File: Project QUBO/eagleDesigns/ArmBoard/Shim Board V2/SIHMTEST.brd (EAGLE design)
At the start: 71.1 x 81.3 mm, 30 parts, among them IC1 MCP2551/SN, U1 BME280

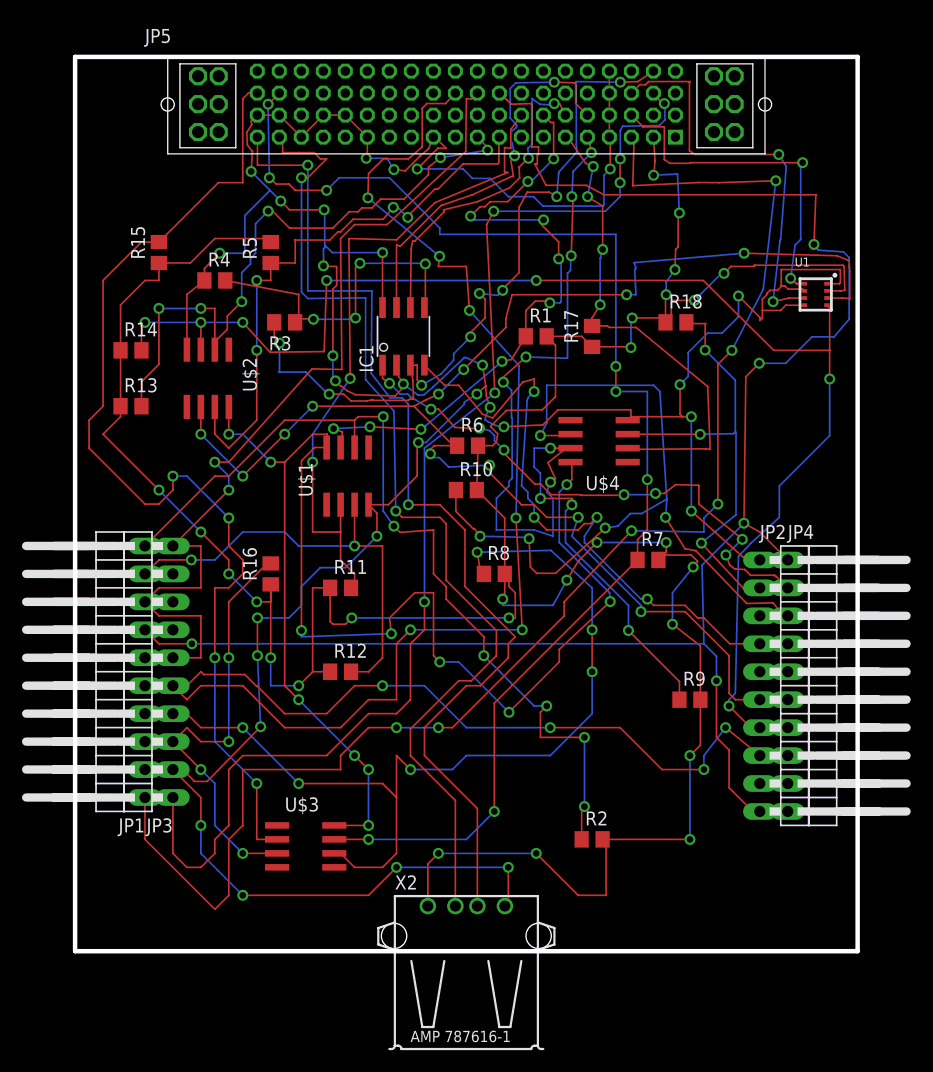
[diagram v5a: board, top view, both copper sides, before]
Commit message: 
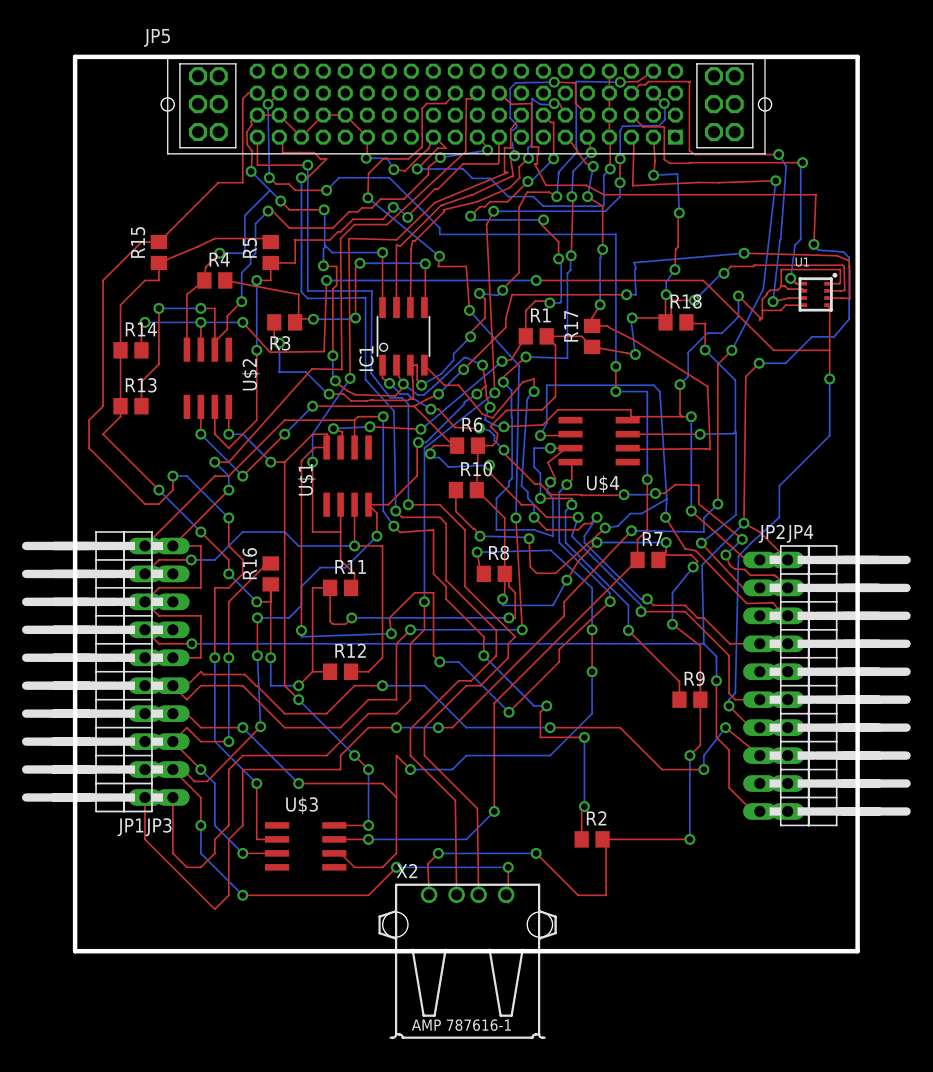
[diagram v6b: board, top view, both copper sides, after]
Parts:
- moved X2 1.04 mm to (35.7, -7.86)
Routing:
- net USB-: track 92.9 -> 91.9 mm
- net USB+: track 94.1 -> 93.0 mm
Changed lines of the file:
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@@
 <attribute name="PROD_ID" value="IC-13090" x="67.31" y="59.69" size="1.778" layer="27" display="off"/>
 </element>
-<element name="X2" library="con-amp" package="USB" value="" x="35.56" y="-8.89"/>
+<element name="X2" library="con-amp" package="USB" value="" x="35.6743" y="-7.8613"/>
 </elements>
 <signals>
@@
 <contactref element="X2" pad="3"/>
 <contactref element="JP5" pad="20"/>
-<wire x1="36.56" y1="4.1001" x2="36.56" y2="12.97" width="0.1524" layer="1"/>
+<wire x1="36.6743" y1="5.1288" x2="36.56" y2="12.97" width="0.1524" layer="1"/>
 <wire x1="36.56" y1="12.97" x2="31.75" y2="17.78" width="0.1524" layer="1"/>
 <wire x1="31.75" y1="17.78" x2="31.75" y2="20.32" width="0.1524" layer="1"/>
@@
 <contactref element="X2" pad="2"/>
 <contactref element="JP5" pad="19"/>
-<wire x1="34.56" y1="4.1001" x2="34.56" y2="13.7" width="0.1524" layer="1"/>
+<wire x1="34.6743" y1="5.1288" x2="34.56" y2="13.7" width="0.1524" layer="1"/>
 <wire x1="34.56" y1="13.7" x2="30.48" y2="17.78" width="0.1524" layer="1"/>
 <wire x1="30.48" y1="17.78" x2="30.48" y2="20.193" width="0.1524" layer="1"/>
@@
 <wire x1="6.35" y1="60.96" x2="7.62" y2="60.96" width="0.1524" layer="1"/>
 <wire x1="7.62" y1="60.96" x2="7.62" y2="62.55" width="0.1524" layer="1"/>
-<wire x1="7.62" y1="62.55" x2="10.48" y2="62.55" width="0.1524" layer="1"/>
-<wire x1="10.48" y1="62.55" x2="12.7" y2="64.77" width="0.1524" layer="1"/>
+<wire x1="7.62" y1="62.55" x2="11.1658" y2="64.0359" width="0.1524" layer="1"/>
+<wire x1="11.1658" y1="64.0359" x2="12.7" y2="64.77" width="0.1524" layer="1"/>
 <wire x1="12.7" y1="64.77" x2="17.36" y2="64.77" width="0.1524" layer="1"/>
 <wire x1="4.13" y1="49.53" x2="4.13" y2="48.58" width="0.1524" layer="1"/>
@@
 <wire x1="17.78" y1="31.75" x2="17.78" y2="33.34" width="0.1524" layer="1"/>
 <wire x1="4.13" y1="49.53" x2="4.13" y2="54.61" width="0.1524" layer="1"/>
-<wire x1="32.0599" y1="4.1001" x2="32.0599" y2="7.9299" width="0.1524" layer="1"/>
+<wire x1="32.1742" y1="5.1288" x2="32.0599" y2="7.9299" width="0.1524" layer="1"/>
 <wire x1="32.0599" y1="7.9299" x2="33.02" y2="8.89" width="0.1524" layer="1"/>
 <via x="33.02" y="8.89" extent="1-16" drill="0.6"/>
@@
 <wire x1="69.78015" y1="62.35065" x2="61.77915" y2="62.35065" width="0.1524" layer="1"/>
 <wire x1="61.77915" y1="62.35065" x2="61.66485" y2="62.23635" width="0.1524" layer="1"/>
-<wire x1="46.99" y1="54.93" x2="50.4546" y2="54.93" width="0.1524" layer="1"/>
-<wire x1="50.4546" y1="54.93" x2="50.5206" y2="54.864" width="0.1524" layer="1"/>
-<via x="50.5206" y="54.864" extent="1-16" drill="0.6"/>
-<wire x1="50.5206" y1="54.864" x2="50.5206" y2="57.43575" width="0.1524" layer="16"/>
+<wire x1="46.99" y1="54.93" x2="50.16885" y2="54.3585" width="0.1524" layer="1"/>
+<wire x1="50.16885" y1="54.3585" x2="50.92065" y2="54.23535" width="0.1524" layer="1"/>
+<via x="50.92065" y="54.23535" extent="1-16" drill="0.6"/>
+<wire x1="50.92065" y1="54.23535" x2="50.5206" y2="57.43575" width="0.1524" layer="16"/>
 <wire x1="50.5206" y1="57.43575" x2="50.6349" y2="57.55005" width="0.1524" layer="16"/>
 <via x="50.6349" y="57.55005" extent="1-16" drill="0.6"/>
@@
 <via x="39.37" y="7.62" extent="1-16" drill="0.6"/>
 <wire x1="39.37" y1="7.62" x2="39.37" y2="4.41" width="0.1524" layer="1"/>
-<wire x1="39.37" y1="4.41" x2="39.0601" y2="4.1001" width="0.1524" layer="1"/>
+<wire x1="39.37" y1="4.41" x2="39.1744" y2="5.1288" width="0.1524" layer="1"/>
 <wire x1="10.16" y1="54.67" x2="10.16" y2="59.69" width="0.1524" layer="1"/>
 <wire x1="10.16" y1="59.69" x2="11.75" y2="60.96" width="0.1524" layer="1"/>
@@
 <wire x1="27.432" y1="37.719" x2="27.432" y2="39.818" width="0.1524" layer="1"/>
 <wire x1="27.432" y1="39.818" x2="26.67" y2="40.58" width="0.1524" layer="1"/>
-<wire x1="11.75" y1="60.96" x2="11.75" y2="62.042" width="0.1524" layer="1"/>
-<wire x1="11.75" y1="62.042" x2="13.1445" y2="63.4365" width="0.1524" layer="1"/>
+<wire x1="11.75" y1="60.96" x2="11.8643" y2="62.1563" width="0.1524" layer="1"/>
+<wire x1="11.8643" y1="62.1563" x2="13.1445" y2="63.4365" width="0.1524" layer="1"/>
 <via x="13.1445" y="63.4365" extent="1-16" drill="0.6"/>
 <wire x1="13.1445" y1="63.4365" x2="15.4305" y2="63.4365" width="0.1524" layer="16"/>
@@
 <wire x1="46.99" y1="56.83" x2="48.38315" y2="56.83" width="0.1524" layer="1"/>
 <wire x1="48.38315" y1="56.83" x2="48.52035" y2="56.6928" width="0.1524" layer="1"/>
-<wire x1="48.52035" y1="56.6928" x2="50.9778" y2="56.6928" width="0.1524" layer="1"/>
-<wire x1="50.9778" y1="56.6928" x2="57.4929" y2="51.3207" width="0.1524" layer="1"/>
+<wire x1="48.52035" y1="56.6928" x2="50.69205" y2="55.60695" width="0.1524" layer="1"/>
+<wire x1="50.69205" y1="55.60695" x2="57.4929" y2="51.3207" width="0.1524" layer="1"/>
 <wire x1="57.4929" y1="51.3207" x2="57.7215" y2="45.6057" width="0.1524" layer="1"/>
 <wire x1="57.7215" y1="45.6057" x2="57.32145" y2="45.66285" width="0.1524" layer="1"/>

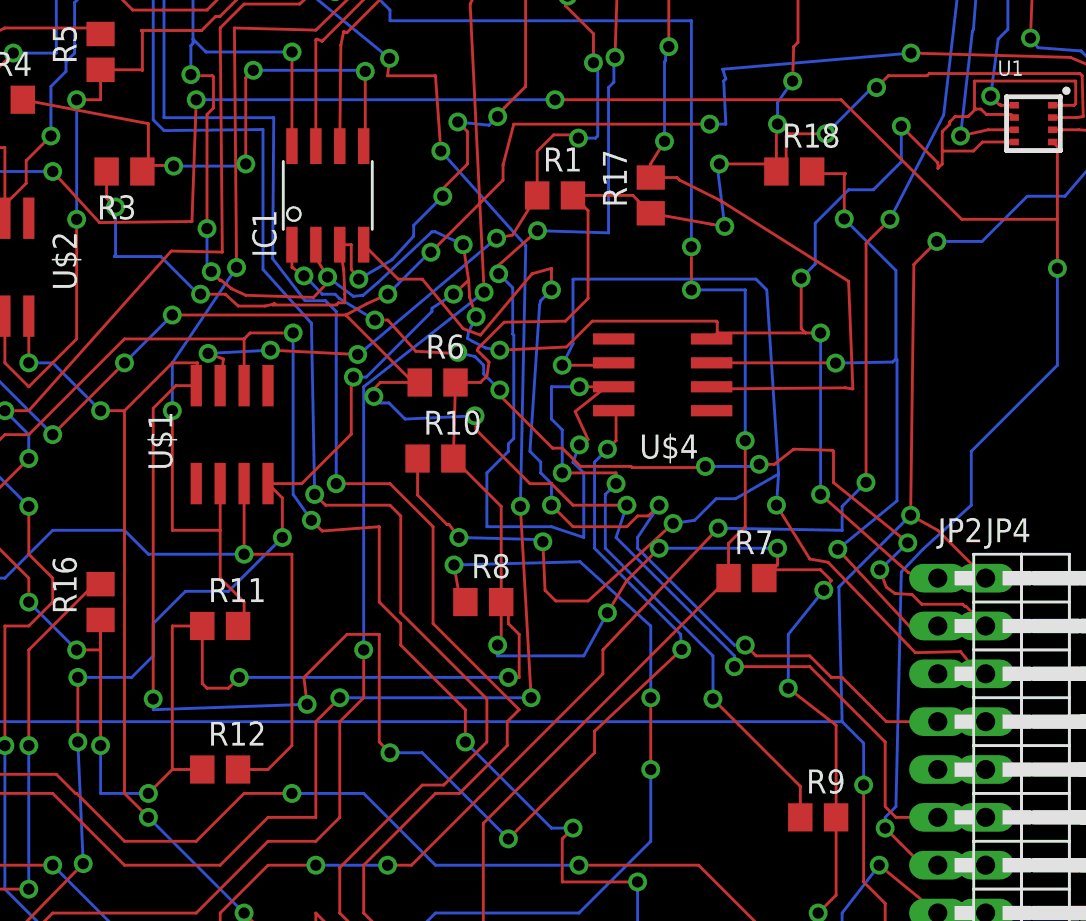
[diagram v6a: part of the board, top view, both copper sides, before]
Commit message: 
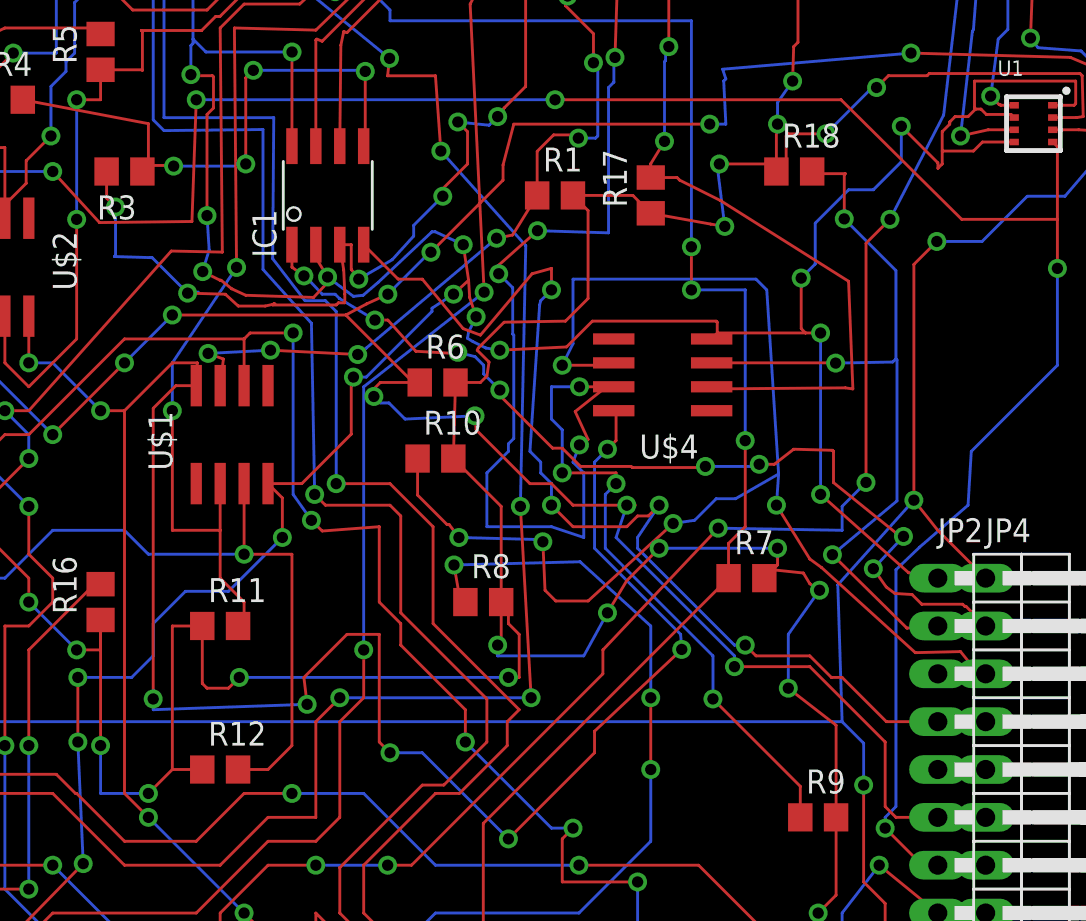
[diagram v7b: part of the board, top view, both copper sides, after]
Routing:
- net 5.0(BME): track 277.5 -> 276.3 mm
- net VDD: track 68.4 -> 69.0 mm
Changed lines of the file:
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@@
 <via x="54.2925" y="29.718" extent="1-16" drill="0.6"/>
 <wire x1="54.2925" y1="29.718" x2="54.2925" y2="32.5755" width="0.1524" layer="16"/>
-<wire x1="54.2925" y1="32.5755" x2="56.17845" y2="34.91865" width="0.1524" layer="16"/>
-<via x="56.17845" y="34.91865" extent="1-16" drill="0.6"/>
-<wire x1="56.17845" y1="34.91865" x2="56.5785" y2="35.433" width="0.1524" layer="1"/>
-<wire x1="56.5785" y1="35.433" x2="56.007" y2="36.0045" width="0.1524" layer="1"/>
-<wire x1="56.007" y1="36.0045" x2="53.4645" y2="36.0045" width="0.1524" layer="1"/>
+<wire x1="54.2925" y1="32.5755" x2="55.94985" y2="34.91865" width="0.1524" layer="16"/>
+<via x="55.94985" y="34.91865" extent="1-16" drill="0.6"/>
+<wire x1="55.94985" y1="34.91865" x2="55.4355" y2="35.26155" width="0.1524" layer="1"/>
+<wire x1="55.4355" y1="35.26155" x2="55.0926" y2="35.83305" width="0.1524" layer="1"/>
+<wire x1="55.0926" y1="35.83305" x2="53.4645" y2="36.0045" width="0.1524" layer="1"/>
 <wire x1="53.4645" y1="36.0045" x2="53.02" y2="35.56" width="0.1524" layer="1"/>
 <wire x1="36.51" y1="41.91" x2="36.6243" y2="45.9486" width="0.1524" layer="1"/>
@@
 <wire x1="56.6928" y1="42.291" x2="56.6928" y2="40.63365" width="0.1524" layer="1"/>
 <wire x1="56.6928" y1="40.63365" x2="60.2361" y2="37.77615" width="0.1524" layer="1"/>
-<wire x1="60.2361" y1="37.77615" x2="60.63615" y2="37.43325" width="0.1524" layer="1"/>
-<via x="60.63615" y="37.43325" extent="1-16" drill="0.6"/>
-<wire x1="60.63615" y1="37.43325" x2="59.15025" y2="36.0045" width="0.1524" layer="16"/>
-<via x="59.15025" y="36.0045" extent="1-16" drill="0.6"/>
-<wire x1="59.15025" y1="36.0045" x2="59.49315" y2="35.0901" width="0.1524" layer="1"/>
+<wire x1="60.2361" y1="37.77615" x2="60.40755" y2="37.77615" width="0.1524" layer="1"/>
+<via x="60.40755" y="37.77615" extent="1-16" drill="0.6"/>
+<wire x1="60.40755" y1="37.77615" x2="58.80735" y2="36.06165" width="0.1524" layer="16"/>
+<via x="58.80735" y="36.06165" extent="1-16" drill="0.6"/>
+<wire x1="58.80735" y1="36.06165" x2="59.49315" y2="35.0901" width="0.1524" layer="1"/>
 <wire x1="59.49315" y1="35.0901" x2="59.95035" y2="34.7472" width="0.1524" layer="1"/>
 <wire x1="59.95035" y1="34.7472" x2="60.86475" y2="34.69005" width="0.1524" layer="1"/>
@@
 <wire x1="24.74595" y1="50.92065" x2="24.17445" y2="51.37785" width="0.1524" layer="1"/>
 <wire x1="24.17445" y1="51.37785" x2="24.1173" y2="51.37785" width="0.1524" layer="1"/>
-<wire x1="24.1173" y1="51.37785" x2="23.6601" y2="51.83505" width="0.1524" layer="1"/>
-<via x="23.6601" y="51.83505" extent="1-16" drill="0.6"/>
-<wire x1="23.6601" y1="51.83505" x2="23.7744" y2="51.5493" width="0.1524" layer="16"/>
-<wire x1="23.7744" y1="51.5493" x2="23.4315" y2="51.8922" width="0.1524" layer="16"/>
-<wire x1="23.4315" y1="51.8922" x2="23.4315" y2="54.12105" width="0.1524" layer="16"/>
-<via x="23.4315" y="54.12105" extent="1-16" drill="0.6"/>
-<wire x1="23.4315" y1="54.12105" x2="23.4315" y2="60.17895" width="0.1524" layer="1"/>
+<wire x1="24.1173" y1="51.37785" x2="23.2029" y2="51.83505" width="0.1524" layer="1"/>
+<via x="23.2029" y="51.83505" extent="1-16" drill="0.6"/>
+<wire x1="23.2029" y1="51.83505" x2="23.26005" y2="52.06365" width="0.1524" layer="16"/>
+<wire x1="23.26005" y1="52.06365" x2="23.5458" y2="52.97805" width="0.1524" layer="16"/>
+<wire x1="23.5458" y1="52.97805" x2="23.4315" y2="54.80685" width="0.1524" layer="16"/>
+<via x="23.4315" y="54.80685" extent="1-16" drill="0.6"/>
+<wire x1="23.4315" y1="54.80685" x2="23.4315" y2="60.17895" width="0.1524" layer="1"/>
 <wire x1="23.4315" y1="60.17895" x2="23.7744" y2="60.52185" width="0.1524" layer="1"/>
 <wire x1="23.7744" y1="60.52185" x2="23.7744" y2="62.1792" width="0.1524" layer="1"/>
@@
 <wire x1="59.436" y1="22.2885" x2="59.436" y2="22.86" width="0.1524" layer="16"/>
 <wire x1="59.436" y1="22.86" x2="60.0075" y2="23.4315" width="0.1524" layer="16"/>
-<wire x1="60.0075" y1="23.4315" x2="60.29325" y2="35.8902" width="0.1524" layer="16"/>
-<wire x1="60.29325" y1="35.8902" x2="61.43625" y2="37.09035" width="0.1524" layer="16"/>
-<wire x1="61.43625" y1="37.09035" x2="64.008" y2="39.4335" width="0.1524" layer="16"/>
-<wire x1="64.008" y1="39.4335" x2="64.008" y2="42.291" width="0.1524" layer="16"/>
+<wire x1="60.0075" y1="23.4315" x2="60.0075" y2="36.0045" width="0.1524" layer="16"/>
+<wire x1="60.0075" y1="36.0045" x2="61.2648" y2="37.20465" width="0.1524" layer="16"/>
+<wire x1="61.2648" y1="37.20465" x2="63.83655" y2="39.4335" width="0.1524" layer="16"/>
+<wire x1="63.83655" y1="39.4335" x2="64.008" y2="42.291" width="0.1524" layer="16"/>
 <wire x1="64.008" y1="42.291" x2="68.58" y2="46.863" width="0.1524" layer="16"/>
 <wire x1="68.58" y1="46.863" x2="68.58" y2="52.0065" width="0.1524" layer="16"/>
@@
 <contactref element="U$4" pad="3"/>
 <contactref element="R18" pad="2"/>
-<wire x1="62.23" y1="33.02" x2="60.76315" y2="32.96285" width="0.1524" layer="1"/>
-<wire x1="60.76315" y1="32.96285" x2="56.9214" y2="37.09035" width="0.1524" layer="1"/>
-<via x="56.9214" y="37.09035" extent="1-16" drill="0.6"/>
-<wire x1="56.9214" y1="37.09035" x2="60.06465" y2="39.6621" width="0.1524" layer="16"/>
+<wire x1="62.23" y1="33.02" x2="60.5917" y2="32.9057" width="0.1524" layer="1"/>
+<wire x1="60.5917" y1="32.9057" x2="56.63565" y2="36.8046" width="0.1524" layer="1"/>
+<via x="56.63565" y="36.8046" extent="1-16" drill="0.6"/>
+<wire x1="56.63565" y1="36.8046" x2="60.06465" y2="39.6621" width="0.1524" layer="16"/>
 <wire x1="60.06465" y1="39.6621" x2="60.06465" y2="47.14875" width="0.1524" layer="16"/>
 <wire x1="60.06465" y1="47.14875" x2="60.0075" y2="47.2059" width="0.1524" layer="16"/>
@@
 <wire x1="64.389" y1="30.48" x2="63.4365" y2="31.6611" width="0.1524" layer="1"/>
 <wire x1="63.4365" y1="31.6611" x2="61.0362" y2="31.60395" width="0.1524" layer="1"/>
-<wire x1="61.0362" y1="31.60395" x2="56.40705" y2="36.40455" width="0.1524" layer="1"/>
-<wire x1="56.40705" y1="36.40455" x2="55.4355" y2="36.576" width="0.1524" layer="1"/>
+<wire x1="61.0362" y1="31.60395" x2="56.06415" y2="36.1188" width="0.1524" layer="1"/>
+<wire x1="56.06415" y1="36.1188" x2="55.4355" y2="36.576" width="0.1524" layer="1"/>
 <wire x1="55.4355" y1="36.576" x2="53.66385" y2="39.4335" width="0.1524" layer="1"/>
 <via x="53.66385" y="39.4335" extent="1-16" drill="0.6"/>
@@
 <via x="10.6172" y="27.94" extent="1-16" drill="0.6"/>
 <wire x1="10.6172" y1="27.94" x2="57.15" y2="27.94" width="0.1524" layer="16"/>
-<wire x1="57.15" y1="27.94" x2="56.97855" y2="35.0901" width="0.1524" layer="16"/>
-<wire x1="56.97855" y1="35.0901" x2="60.78855" y2="38.9001" width="0.1524" layer="16"/>
-<via x="60.78855" y="38.9001" extent="1-16" drill="0.6"/>
-<wire x1="60.78855" y1="38.9001" x2="62.23" y2="38.1" width="0.1524" layer="1"/>
+<wire x1="57.15" y1="27.94" x2="56.9214" y2="35.2044" width="0.1524" layer="16"/>
+<wire x1="56.9214" y1="35.2044" x2="60.96" y2="39.7002" width="0.1524" layer="16"/>
+<via x="60.96" y="39.7002" extent="1-16" drill="0.6"/>
+<wire x1="60.96" y1="39.7002" x2="62.23" y2="38.1" width="0.1524" layer="1"/>
 <wire x1="62.23" y1="38.1" x2="64.77" y2="35.56" width="0.1524" layer="1"/>
 <wire x1="62.23" y1="12.7" x2="61.595" y2="12.7" width="0.1524" layer="1"/>
@@
 <wire x1="58.293" y1="24.5745" x2="58.293" y2="26.797" width="0.1524" layer="16"/>
 <wire x1="58.293" y1="26.797" x2="57.15" y2="27.94" width="0.1524" layer="16"/>
-<wire x1="60.78855" y1="38.9001" x2="60.96" y2="52.21605" width="0.1524" layer="1"/>
+<wire x1="60.96" y1="39.7002" x2="60.96" y2="52.21605" width="0.1524" layer="1"/>
 <wire x1="60.96" y1="52.21605" x2="62.1792" y2="53.43525" width="0.1524" layer="1"/>
 <via x="62.1792" y="53.43525" extent="1-16" drill="0.6"/>
@@
 <wire x1="18.57375" y1="55.26405" x2="18.57375" y2="52.6923" width="0.1524" layer="16"/>
 <wire x1="18.57375" y1="52.6923" x2="18.5166" y2="52.63515" width="0.1524" layer="16"/>
-<wire x1="18.5166" y1="52.63515" x2="20.97405" y2="52.63515" width="0.1524" layer="16"/>
-<wire x1="20.97405" y1="52.63515" x2="22.91715" y2="50.69205" width="0.1524" layer="16"/>
-<wire x1="22.91715" y1="50.69205" x2="23.03145" y2="50.69205" width="0.1524" layer="16"/>
-<wire x1="23.03145" y1="50.69205" x2="23.0886" y2="50.6349" width="0.1524" layer="16"/>
-<via x="23.0886" y="50.6349" extent="1-16" drill="0.6"/>
-<wire x1="23.0886" y1="50.6349" x2="24.40305" y2="50.6349" width="0.1524" layer="1"/>
+<wire x1="18.5166" y1="52.63515" x2="20.40255" y2="52.578" width="0.1524" layer="16"/>
+<wire x1="22.9743" y1="50.7492" x2="22.4028" y2="50.69205" width="0.1524" layer="16"/>
+<via x="22.4028" y="50.69205" extent="1-16" drill="0.6"/>
+<wire x1="22.4028" y1="50.69205" x2="24.40305" y2="50.6349" width="0.1524" layer="1"/>
 <wire x1="24.40305" y1="50.6349" x2="25.08885" y2="50.00625" width="0.1524" layer="1"/>
 <wire x1="25.08885" y1="50.00625" x2="26.5176" y2="50.00625" width="0.1524" layer="1"/>
@@
 <wire x1="49.54905" y1="78.9813" x2="51.15125" y2="79.03845" width="0.1524" layer="1"/>
 <wire x1="51.15125" y1="79.03845" x2="52.56" y2="79.99" width="0.1524" layer="1"/>
+<wire x1="20.40255" y1="52.578" x2="20.51685" y2="52.578" width="0.1524" layer="16"/>
+<wire x1="20.51685" y1="52.578" x2="22.4028" y2="50.69205" width="0.1524" layer="16"/>
 </signal>
 <signal name="CANRX">
